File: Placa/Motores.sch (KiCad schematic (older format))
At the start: 9 parts, among them U1 DVR8833, U2 DVR8833

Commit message: Se termino la placa, y se mando a fabricar.
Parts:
- C6: footprint Capacitors_SMD:C_0805_HandSoldering -> Capacitors_SMD:C_1206
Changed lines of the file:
@@
 LIBS:DVR8833
 LIBS:sn74lvc2g86
+LIBS:logo
 LIBS:placa-cache
 EELAYER 25 0
@@
 F 0 "C6" H 3925 2250 50  0000 L CNN
 F 1 "10uF" H 3925 2050 50  0000 L CNN
-F 2 "Capacitors_SMD:C_0805_HandSoldering" H 3938 2000 50  0001 C CNN
+F 2 "Capacitors_SMD:C_1206" H 3938 2000 50  0001 C CNN
 F 3 "" H 3900 2150 50  0000 C CNN
 	1    3900 2150

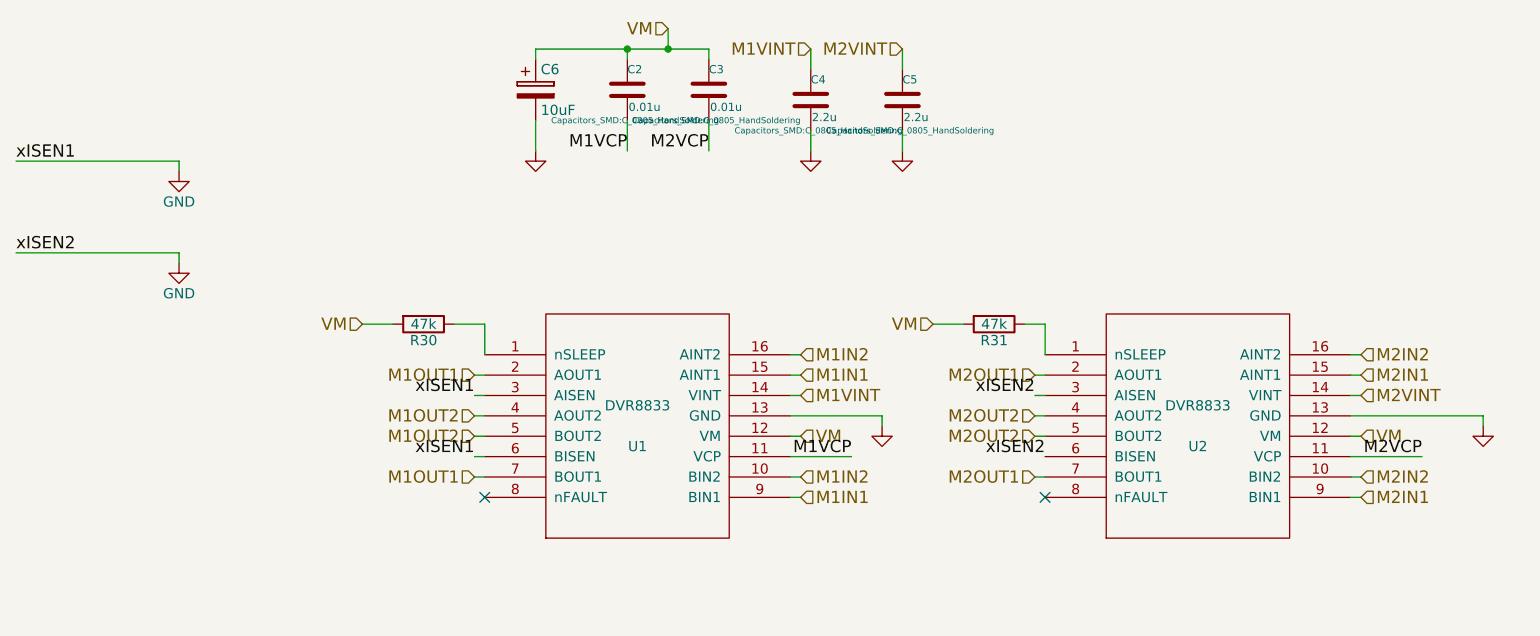
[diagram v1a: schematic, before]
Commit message: Agrego cambios sugeridos en la wiki de github.
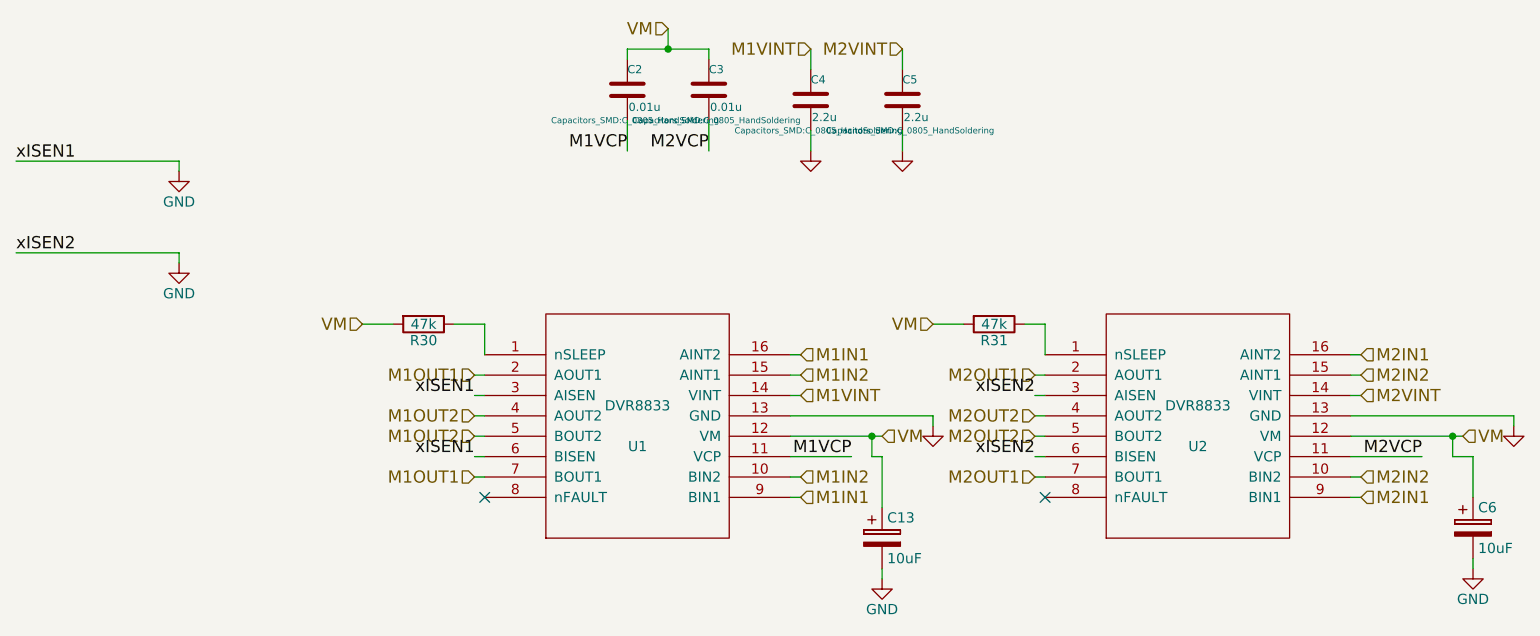
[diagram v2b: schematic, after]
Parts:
- added C13: 10uF, Capacitors_SMD:C_1206, symbol CP
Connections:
- net GND: now also C13.2
- net M1IN1: now also U1.16 (AINT2); no longer U1.15 (AINT1)
- net M1IN2: now also U1.15 (AINT1); no longer U1.16 (AINT2)
- net M2IN1: now also U2.16 (AINT2); no longer U2.15 (AINT1)
- net M2IN2: now also U2.15 (AINT1); no longer U2.16 (AINT2)
- net VM: now also C13.1
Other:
- moved on the sheet: C6
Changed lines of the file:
@@
 LIBS:DVR8833
 LIBS:sn74lvc2g86
-LIBS:logo
-LIBS:placa-cache
 EELAYER 25 0
 EELAYER END
@@
 L GND #PWR040
 U 1 1 55EB047B
-P 5600 3800
-F 0 "#PWR040" H 5600 3800 30  0001 C CNN
-F 1 "GND" H 5600 3730 30  0001 C CNN
-F 2 "" H 5600 3800 60  0000 C CNN
-F 3 "" H 5600 3800 60  0000 C CNN
-	1    5600 3800
+P 5850 3800
+F 0 "#PWR040" H 5850 3800 30  0001 C CNN
+F 1 "GND" H 5850 3730 30  0001 C CNN
+F 2 "" H 5850 3800 60  0000 C CNN
+F 3 "" H 5850 3800 60  0000 C CNN
+	1    5850 3800
 	1    0    0    -1
 $EndComp
@@
 L GND #PWR041
 U 1 1 55EB0487
-P 8550 3800
-F 0 "#PWR041" H 8550 3800 30  0001 C CNN
-F 1 "GND" H 8550 3730 30  0001 C CNN
-F 2 "" H 8550 3800 60  0000 C CNN
-F 3 "" H 8550 3800 60  0000 C CNN
-	1    8550 3800
+P 8700 3800
+F 0 "#PWR041" H 8700 3800 30  0001 C CNN
+F 1 "GND" H 8700 3730 30  0001 C CNN
+F 2 "" H 8700 3800 60  0000 C CNN
+F 3 "" H 8700 3800 60  0000 C CNN
+	1    8700 3800
 	1    0    0    -1
 $EndComp
@@
 	5150 4050 5200 4050
 Wire Wire Line
-	5150 3850 5200 3850
-Wire Wire Line
-	5150 3750 5600 3750
-Wire Wire Line
-	5600 3750 5600 3800
+	5150 3850 5600 3850
+Wire Wire Line
+	5150 3750 5850 3750
+Wire Wire Line
+	5850 3750 5850 3800
 Wire Wire Line
 	5150 3950 5450 3950
@@
 	7900 3550 7950 3550
 Wire Wire Line
-	7900 3750 8550 3750
-Wire Wire Line
-	8550 3750 8550 3800
-Wire Wire Line
-	7900 3850 7950 3850
+	7900 3750 8700 3750
+Wire Wire Line
+	8700 3750 8700 3800
+Wire Wire Line
+	7900 3850 8450 3850
 Wire Wire Line
 	7900 3950 8250 3950
-Wire Wire Line
-	3900 1950 4750 1950
 Wire Wire Line
 	4550 1850 4550 1950
 Connection ~ 4550 1950
 Wire Wire Line
-	4750 2300 4750 2450
+	4750 2450 4750 2300
 Wire Wire Line
 	4350 2300 4350 2450
 $Comp
 L GND #PWR042
-U 1 1 55EB1201
-P 3900 2450
-F 0 "#PWR042" H 3900 2450 30  0001 C CNN
-F 1 "GND" H 3900 2380 30  0001 C CNN
-F 2 "" H 3900 2450 60  0000 C CNN
-F 3 "" H 3900 2450 60  0000 C CNN
-	1    3900 2450
-	1    0    0    -1
-$EndComp
-$Comp
-L GND #PWR043
 U 1 1 55EB12DF
 P 5250 2450
-F 0 "#PWR043" H 5250 2450 30  0001 C CNN
+F 0 "#PWR042" H 5250 2450 30  0001 C CNN
 F 1 "GND" H 5250 2380 30  0001 C CNN
 F 2 "" H 5250 2450 60  0000 C CNN
@@
 $EndComp
 $Comp
-L GND #PWR044
+L GND #PWR043
 U 1 1 55EB12E5
 P 5700 2450
-F 0 "#PWR044" H 5700 2450 30  0001 C CNN
+F 0 "#PWR043" H 5700 2450 30  0001 C CNN
 F 1 "GND" H 5700 2380 30  0001 C CNN
 F 2 "" H 5700 2450 60  0000 C CNN
@@
 Wire Wire Line
 	7900 4150 7950 4150
-Connection ~ 4350 1950
-Wire Wire Line
-	3900 2300 3900 2450
 Wire Wire Line
 	4350 2000 4350 1950
@@
 L CP C6
 U 1 1 571AC7CC
-P 3900 2150
-F 0 "C6" H 3925 2250 50  0000 L CNN
-F 1 "10uF" H 3925 2050 50  0000 L CNN
-F 2 "Capacitors_SMD:C_1206" H 3938 2000 50  0001 C CNN
-F 3 "" H 3900 2150 50  0000 C CNN
-	1    3900 2150
-	1    0    0    -1
-$EndComp
-Wire Wire Line
-	3900 2000 3900 1950
+P 8500 4300
+F 0 "C6" H 8525 4400 50  0000 L CNN
+F 1 "10uF" H 8525 4200 50  0000 L CNN
+F 2 "Capacitors_SMD:C_1206" H 8538 4150 50  0001 C CNN
+F 3 "" H 8500 4300 50  0000 C CNN
+	1    8500 4300
+	1    0    0    -1
+$EndComp
+Text HLabel 7950 3550 2    60   Input ~ 0
+M2IN2
 Text HLabel 7950 3450 2    60   Input ~ 0
-M2IN2
-Text HLabel 7950 3550 2    60   Input ~ 0
 M2IN1
 Text HLabel 7950 3650 2    60   Input ~ 0
 M2VINT
-Text HLabel 7950 3850 2    60   Input ~ 0
+Text HLabel 8450 3850 2    60   Input ~ 0
 VM
 Text HLabel 7950 4050 2    60   Input ~ 0
@@
 Text HLabel 6350 4050 0    60   Input ~ 0
 M2OUT1
+Text HLabel 5200 3550 2    60   Input ~ 0
+M1IN2
 Text HLabel 5200 3450 2    60   Input ~ 0
-M1IN2
-Text HLabel 5200 3550 2    60   Input ~ 0
 M1IN1
 Text HLabel 5200 3650 2    60   Input ~ 0
 M1VINT
-Text HLabel 5200 3850 2    60   Input ~ 0
+Text HLabel 5600 3850 2    60   Input ~ 0
 VM
 Text HLabel 5200 4050 2    60   Input ~ 0
@@
 	2150 2500 2150 2550
 $Comp
-L GND #PWR045
+L GND #PWR044
 U 1 1 5749021E
 P 2150 2550
-F 0 "#PWR045" H 2150 2300 50  0001 C CNN
+F 0 "#PWR044" H 2150 2300 50  0001 C CNN
 F 1 "GND" H 2150 2400 50  0000 C CNN
 F 2 "" H 2150 2550 50  0000 C CNN
@@
 	2150 2950 2150 3000
 $Comp
-L GND #PWR046
+L GND #PWR045
 U 1 1 574909F4
 P 2150 3000
-F 0 "#PWR046" H 2150 2750 50  0001 C CNN
+F 0 "#PWR045" H 2150 2750 50  0001 C CNN
 F 1 "GND" H 2150 2850 50  0000 C CNN
 F 2 "" H 2150 3000 50  0000 C CNN
@@
 Text Label 6350 3650 2    60   ~ 0
 xISEN2
-Text Label 6400 3950 2    60   ~ 0
+Text Label 6350 3950 2    60   ~ 0
 xISEN2
 NoConn ~ 3650 4150
@@
 Wire Wire Line
 	3050 3300 3200 3300
+$Comp
+L CP C13
+U 1 1 585474A3
+P 5600 4350
+F 0 "C13" H 5625 4450 50  0000 L CNN
+F 1 "10uF" H 5625 4250 50  0000 L CNN
+F 2 "Capacitors_SMD:C_1206" H 5638 4200 50  0001 C CNN
+F 3 "" H 5600 4350 50  0000 C CNN
+	1    5600 4350
+	1    0    0    -1
+$EndComp
+Wire Wire Line
+	4350 1950 4750 1950
+Wire Wire Line
+	5550 3850 5550 3950
+Wire Wire Line
+	5550 3950 5600 3950
+Wire Wire Line
+	5600 3950 5600 4200
+Connection ~ 5550 3850
+Wire Wire Line
+	5600 4500 5600 4550
+$Comp
+L GND #PWR046
+U 1 1 585479F8
+P 5600 4550
+F 0 "#PWR046" H 5600 4300 50  0001 C CNN
+F 1 "GND" H 5600 4400 50  0000 C CNN
+F 2 "" H 5600 4550 50  0000 C CNN
+F 3 "" H 5600 4550 50  0000 C CNN
+	1    5600 4550
+	1    0    0    -1
+$EndComp
+Wire Wire Line
+	8400 3850 8400 3950
+Wire Wire Line
+	8400 3950 8500 3950
+Wire Wire Line
+	8500 3950 8500 4150
+Connection ~ 8400 3850
+Wire Wire Line
+	8500 4450 8500 4500
+$Comp
+L GND #PWR047
+U 1 1 58547B09
+P 8500 4500
+F 0 "#PWR047" H 8500 4250 50  0001 C CNN
+F 1 "GND" H 8500 4350 50  0000 C CNN
+F 2 "" H 8500 4500 50  0000 C CNN
+F 3 "" H 8500 4500 50  0000 C CNN
+	1    8500 4500
+	1    0    0    -1
+$EndComp
+Wire Wire Line
+	6350 3950 6400 3950
 $EndSCHEMATC
